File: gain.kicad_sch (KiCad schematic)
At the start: 7 parts, among them U4 TL074

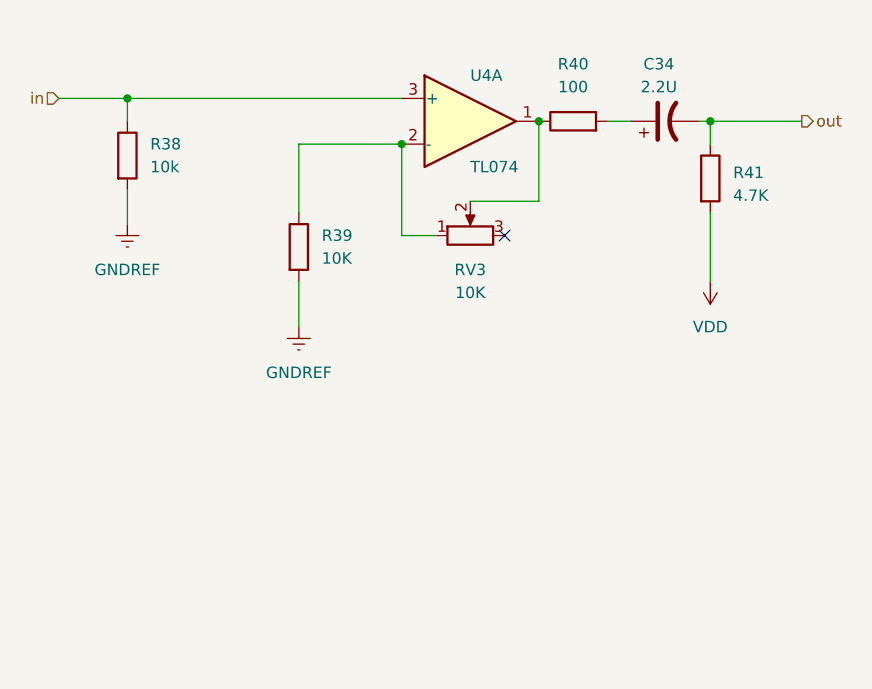
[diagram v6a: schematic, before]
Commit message: fix gain stage for DC offset and some changes to power filtration
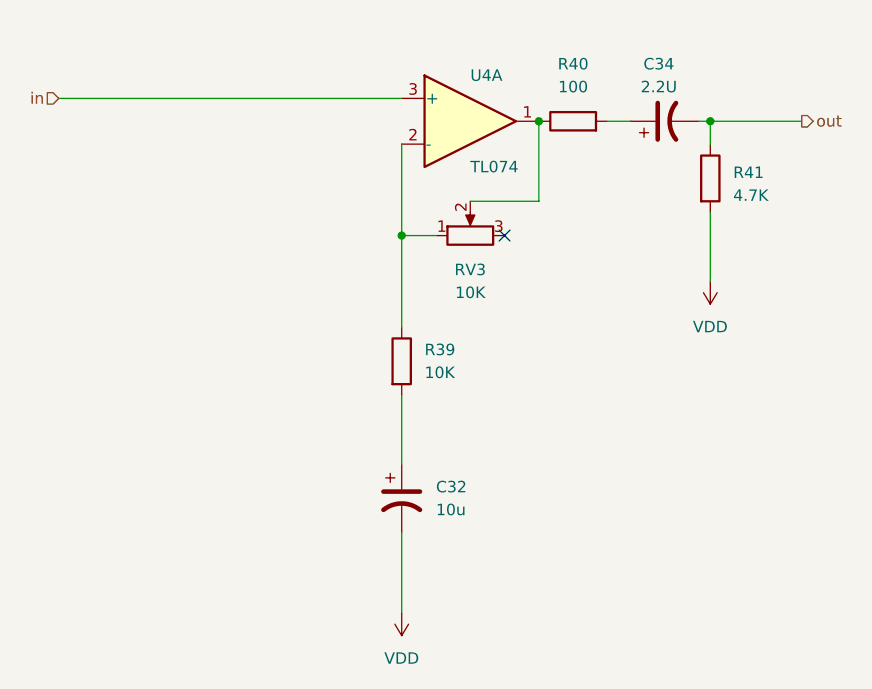
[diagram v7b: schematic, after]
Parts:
- removed R38: 10k, Resistor_SMD:R_1206_3216Metric_Pad1.30x1.75mm_HandSolder, symbol Device:R
- added C32: 10u, Capacitor_THT:CP_Radial_D5.0mm_P2.50mm, symbol Device:C_Polarized_US
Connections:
- net VDD: now also C32.2
- net GNDREF: no longer names the net of R39.2
- net GNDREF: now also C32.1
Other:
- moved on the sheet: R39
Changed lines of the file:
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@@
   (junction (at 116.84 68.58) (diameter 0) (color 0 0 0 0)
   )
-  (junction (at 71.12 66.04) (diameter 0) (color 0 0 0 0)
-  )
-  (junction (at 101.6 71.12) (diameter 0) (color 0 0 0 0)
+  (junction (at 101.6 81.28) (diameter 0) (color 0 0 0 0)
   )
   (junction (at 135.89 68.58) (diameter 0) (color 0 0 0 0)
   )
   (no_connect (at 113.03 81.28))
+  (wire (pts (xy 101.6 114.3) (xy 101.6 123.19))
+    (stroke (width 0) (type default))
+  )
   (wire (pts (xy 135.89 68.58) (xy 135.89 71.12))
     (stroke (width 0) (type default))
   )
-  (wire (pts (xy 90.17 86.36) (xy 90.17 91.44))
-    (stroke (width 0) (type default))
-  )
-  (wire (pts (xy 90.17 71.12) (xy 101.6 71.12))
-    (stroke (width 0) (type default))
-  )
-  (wire (pts (xy 90.17 78.74) (xy 90.17 71.12))
-    (stroke (width 0) (type default))
-  )
   (wire (pts (xy 134.62 68.58) (xy 135.89 68.58))
     (stroke (width 0) (type default))
@@
     (stroke (width 0) (type default))
   )
-  (wire (pts (xy 71.12 76.2) (xy 71.12 80.01))
-    (stroke (width 0) (type default))
-  )
-  (wire (pts (xy 71.12 68.58) (xy 71.12 66.04))
+  (wire (pts (xy 101.6 81.28) (xy 101.6 91.44))
     (stroke (width 0) (type default))
   )
@@
     (stroke (width 0) (type default))
   )
+  (wire (pts (xy 101.6 99.06) (xy 101.6 106.68))
+    (stroke (width 0) (type default))
+  )
   (wire (pts (xy 116.84 77.47) (xy 109.22 77.47))
     (stroke (width 0) (type default))
   )
-  (wire (pts (xy 63.5 66.04) (xy 71.12 66.04))
-    (stroke (width 0) (type default))
-  )
-  (wire (pts (xy 71.12 66.04) (xy 101.6 66.04))
+  (wire (pts (xy 63.5 66.04) (xy 101.6 66.04))
     (stroke (width 0) (type default))
   )
@@
     )
   )
+  (symbol (lib_id "Device:C_Polarized_US") (at 101.6 110.49 0) (unit 1)
+    (in_bom yes) (on_board yes) (dnp no) (fields_autoplaced)
+    (property "Reference" "C32" (at 105.41 109.22 0)
+      (effects (font (size 1.27 1.27)) (justify left))
+    )
+    (property "Value" "10u" (at 105.41 111.76 0)
+      (effects (font (size 1.27 1.27)) (justify left))
+    )
+    (property "Footprint" "Capacitor_THT:CP_Radial_D5.0mm_P2.50mm" (at 101.6 110.49 0)
+      (effects (font (size 1.27 1.27)) hide)
+    )
+    (property "Datasheet" "~" (at 101.6 110.49 0)
+      (effects (font (size 1.27 1.27)) hide)
+    )
+    (pin "1")
+    (pin "2")
+    (instances
+      (project "crossover"
+        (path "/3c8df2a5-e9f9-4495-af40-aa221f0b3fa5/28472e3b-9819-48c0-b63f-39bc09c5cac5"
+          (reference "C32") (unit 1)
+        )
+        (path "/3c8df2a5-e9f9-4495-af40-aa221f0b3fa5/26fb0579-508e-4f39-8fcc-d72882569c12"
+          (reference "C24") (unit 1)
+        )
+        (path "/3c8df2a5-e9f9-4495-af40-aa221f0b3fa5/8c997b3b-7bf2-44b2-ab14-da860701b424"
+          (reference "C30") (unit 1)
+        )
+        (path "/3c8df2a5-e9f9-4495-af40-aa221f0b3fa5/6a6e002a-0565-47d4-a8fe-a1e284818334"
+          (reference "C36") (unit 1)
+        )
+      )
+    )
+  )
   (symbol (lib_id "Device:C_Polarized_US") (at 130.81 68.58 90) (unit 1)
     (in_bom yes) (on_board yes) (dnp no) (fields_autoplaced)
@@
     )
   )
-  (symbol (lib_id "Device:R") (at 71.12 72.39 0) (unit 1)
-    (in_bom yes) (on_board yes) (dnp no) (fields_autoplaced)
-    (property "Reference" "R38" (at 73.66 71.1199 0)
-      (effects (font (size 1.27 1.27)) (justify left))
-    )
-    (property "Value" "10k" (at 73.66 73.6599 0)
-      (effects (font (size 1.27 1.27)) (justify left))
-    )
-    (property "Footprint" "Resistor_SMD:R_1206_3216Metric_Pad1.30x1.75mm_HandSolder" (at 69.342 72.39 90)
-      (effects (font (size 1.27 1.27)) hide)
-    )
-    (property "Datasheet" "~" (at 71.12 72.39 0)
-      (effects (font (size 1.27 1.27)) hide)
-    )
-    (pin "1")
-    (pin "2")
-    (instances
-      (project "crossover"
-        (path "/3c8df2a5-e9f9-4495-af40-aa221f0b3fa5/28472e3b-9819-48c0-b63f-39bc09c5cac5"
-          (reference "R38") (unit 1)
-        )
-        (path "/3c8df2a5-e9f9-4495-af40-aa221f0b3fa5/8c997b3b-7bf2-44b2-ab14-da860701b424"
-          (reference "R34") (unit 1)
-        )
-        (path "/3c8df2a5-e9f9-4495-af40-aa221f0b3fa5/26fb0579-508e-4f39-8fcc-d72882569c12"
-          (reference "R26") (unit 1)
-        )
-        (path "/3c8df2a5-e9f9-4495-af40-aa221f0b3fa5/6a6e002a-0565-47d4-a8fe-a1e284818334"
-          (reference "R42") (unit 1)
-        )
-      )
-    )
-  )
-  (symbol (lib_id "power:GNDREF") (at 71.12 80.01 0) (unit 1)
-    (in_bom yes) (on_board yes) (dnp no) (fields_autoplaced)
-    (property "Reference" "#PWR040" (at 71.12 86.36 0)
-      (effects (font (size 1.27 1.27)) hide)
-    )
-    (property "Value" "GNDREF" (at 71.12 85.09 0)
-      (effects (font (size 1.27 1.27)))
-    )
-    (property "Footprint" "" (at 71.12 80.01 0)
-      (effects (font (size 1.27 1.27)) hide)
-    )
-    (property "Datasheet" "" (at 71.12 80.01 0)
-      (effects (font (size 1.27 1.27)) hide)
-    )
-    (pin "1")
-    (instances
-      (project "crossover"
-        (path "/3c8df2a5-e9f9-4495-af40-aa221f0b3fa5/28472e3b-9819-48c0-b63f-39bc09c5cac5"
-          (reference "#PWR040") (unit 1)
-        )
-        (path "/3c8df2a5-e9f9-4495-af40-aa221f0b3fa5/8c997b3b-7bf2-44b2-ab14-da860701b424"
-          (reference "#PWR037") (unit 1)
+  (symbol (lib_id "power:VDD") (at 101.6 123.19 180) (unit 1)
+    (in_bom yes) (on_board yes) (dnp no) (fields_autoplaced)
+    (property "Reference" "#PWR026" (at 101.6 119.38 0)
+      (effects (font (size 1.27 1.27)) hide)
+    )
+    (property "Value" "VDD" (at 101.6 128.27 0)
+      (effects (font (size 1.27 1.27)))
+    )
+    (property "Footprint" "" (at 101.6 123.19 0)
+      (effects (font (size 1.27 1.27)) hide)
+    )
+    (property "Datasheet" "" (at 101.6 123.19 0)
+      (effects (font (size 1.27 1.27)) hide)
+    )
+    (pin "1")
+    (instances
+      (project "crossover"
+        (path "/3c8df2a5-e9f9-4495-af40-aa221f0b3fa5/28472e3b-9819-48c0-b63f-39bc09c5cac5"
+          (reference "#PWR026") (unit 1)
         )
         (path "/3c8df2a5-e9f9-4495-af40-aa221f0b3fa5/26fb0579-508e-4f39-8fcc-d72882569c12"
           (reference "#PWR017") (unit 1)
         )
-        (path "/3c8df2a5-e9f9-4495-af40-aa221f0b3fa5/6a6e002a-0565-47d4-a8fe-a1e284818334"
-          (reference "#PWR043") (unit 1)
-        )
-      )
-    )
-  )
-  (symbol (lib_id "power:GNDREF") (at 90.17 91.44 0) (unit 1)
-    (in_bom yes) (on_board yes) (dnp no) (fields_autoplaced)
-    (property "Reference" "#PWR041" (at 90.17 97.79 0)
-      (effects (font (size 1.27 1.27)) hide)
-    )
-    (property "Value" "GNDREF" (at 90.17 96.52 0)
-      (effects (font (size 1.27 1.27)))
-    )
-    (property "Footprint" "" (at 90.17 91.44 0)
-      (effects (font (size 1.27 1.27)) hide)
-    )
-    (property "Datasheet" "" (at 90.17 91.44 0)
-      (effects (font (size 1.27 1.27)) hide)
-    )
-    (pin "1")
-    (instances
-      (project "crossover"
-        (path "/3c8df2a5-e9f9-4495-af40-aa221f0b3fa5/28472e3b-9819-48c0-b63f-39bc09c5cac5"
-          (reference "#PWR041") (unit 1)
-        )
-        (path "/3c8df2a5-e9f9-4495-af40-aa221f0b3fa5/8c997b3b-7bf2-44b2-ab14-da860701b424"
-          (reference "#PWR038") (unit 1)
-        )
-        (path "/3c8df2a5-e9f9-4495-af40-aa221f0b3fa5/26fb0579-508e-4f39-8fcc-d72882569c12"
+        (path "/3c8df2a5-e9f9-4495-af40-aa221f0b3fa5/8c997b3b-7bf2-44b2-ab14-da860701b424"
           (reference "#PWR018") (unit 1)
         )
         (path "/3c8df2a5-e9f9-4495-af40-aa221f0b3fa5/6a6e002a-0565-47d4-a8fe-a1e284818334"
-          (reference "#PWR044") (unit 1)
-        )
-      )
-    )
-  )
-  (symbol (lib_id "Device:R") (at 90.17 82.55 0) (unit 1)
-    (in_bom yes) (on_board yes) (dnp no) (fields_autoplaced)
-    (property "Reference" "R39" (at 92.71 81.2799 0)
-      (effects (font (size 1.27 1.27)) (justify left))
-    )
-    (property "Value" "10K" (at 92.71 83.8199 0)
-      (effects (font (size 1.27 1.27)) (justify left))
-    )
-    (property "Footprint" "Resistor_SMD:R_1206_3216Metric_Pad1.30x1.75mm_HandSolder" (at 88.392 82.55 90)
-      (effects (font (size 1.27 1.27)) hide)
-    )
-    (property "Datasheet" "~" (at 90.17 82.55 0)
-      (effects (font (size 1.27 1.27)) hide)
-    )
+          (reference "#PWR027") (unit 1)
+        )
+      )
+    )
+  )
+  (symbol (lib_id "Device:R") (at 101.6 95.25 0) (unit 1)
+    (in_bom yes) (on_board yes) (dnp no) (fields_autoplaced)
+    (property "Reference" "R39" (at 104.14 93.9799 0)
+      (effects (font (size 1.27 1.27)) (justify left))
+    )
+    (property "Value" "10K" (at 104.14 96.5199 0)
+      (effects (font (size 1.27 1.27)) (justify left))
+    )
+    (property "Footprint" "Resistor_SMD:R_1206_3216Metric_Pad1.30x1.75mm_HandSolder" (at 99.822 95.25 90)
+      (effects (font (size 1.27 1.27)) hide)
+    )
+    (property "Datasheet" "~" (at 101.6 95.25 0)
+      (effects (font (size 1.27 1.27)) hide)
+    )

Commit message: Finished routing
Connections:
- net in: now also U4.10 (+); no longer U4.3 (+)
- net at R40.1, RV3.2: now also U4.8; no longer U4.1
- net at R39.1, RV3.1: now also U4.9 (-); no longer U4.2 (-)
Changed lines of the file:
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@@
     )
   )
-  (symbol (lib_id "Amplifier_Operational:TL074") (at 109.22 68.58 0) (unit 1)
+  (symbol (lib_id "Amplifier_Operational:TL074") (at 109.22 68.58 0) (unit 3)
     (in_bom yes) (on_board yes) (dnp no) (fields_autoplaced)
-    (property "Reference" "U4" (at 109.22 63.5 0)
-      (effects (font (size 1.27 1.27)) (justify left))
+    (property "Reference" "U4" (at 109.22 59.69 0)
+      (effects (font (size 1.27 1.27)))
     )
-    (property "Value" "TL074" (at 109.22 73.66 0)
-      (effects (font (size 1.27 1.27)) (justify left))
+    (property "Value" "TL074" (at 109.22 62.23 0)
+      (effects (font (size 1.27 1.27)))
     )
     (property "Footprint" "Package_SO:SOIC-14_3.9x8.7mm_P1.27mm" (at 107.95 66.04 0)
@@
       (project "crossover"
         (path "/3c8df2a5-e9f9-4495-af40-aa221f0b3fa5/28472e3b-9819-48c0-b63f-39bc09c5cac5"
-          (reference "U4") (unit 1)
+          (reference "U4") (unit 3)
         )
         (path "/3c8df2a5-e9f9-4495-af40-aa221f0b3fa5/8c997b3b-7bf2-44b2-ab14-da860701b424"
@@
         )
         (path "/3c8df2a5-e9f9-4495-af40-aa221f0b3fa5/26fb0579-508e-4f39-8fcc-d72882569c12"
-          (reference "U4") (unit 3)
+          (reference "U4") (unit 1)
         )
         (path "/3c8df2a5-e9f9-4495-af40-aa221f0b3fa5/6a6e002a-0565-47d4-a8fe-a1e284818334"
